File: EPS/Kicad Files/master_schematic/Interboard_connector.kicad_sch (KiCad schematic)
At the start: 1 part, among them J1 Conn_02x20_Odd_Even

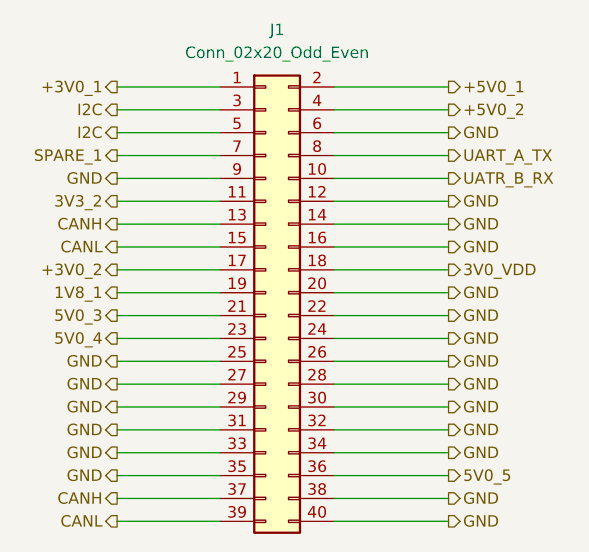
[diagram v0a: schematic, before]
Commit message: revised EPS schematics
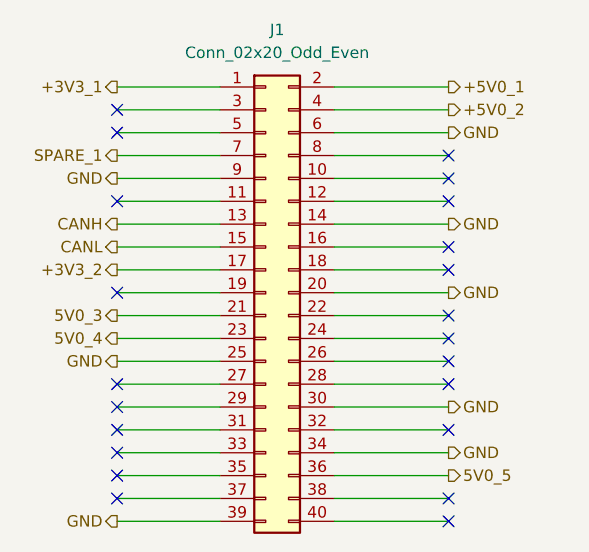
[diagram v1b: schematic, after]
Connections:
- net CANH: no longer J1.37 (Pin_37)
- net CANL: no longer J1.39 (Pin_39)
- net GND: now also J1.39 (Pin_39); no longer J1.12 (Pin_12), J1.16 (Pin_16), J1.22 (Pin_22), J1.24 (Pin_24), J1.26 (Pin_26), J1.27 (Pin_27), J1.28 (Pin_28), J1.29 (Pin_29), J1.31 (Pin_31), J1.32 (Pin_32), J1.33 (Pin_33), J1.35 (Pin_35), J1.38 (Pin_38), J1.40 (Pin_40)
- net +3V0_1 renamed +3V3_1
- net +3V0_2 renamed +3V3_2
- net 1V8_1: no longer names the net of J1.19 (Pin_19)
- net 3V0_VDD: no longer names the net of J1.18 (Pin_18)
- net 3V3_2: no longer names the net of J1.11 (Pin_11)
- net I2C: no longer names the net of J1.3 (Pin_3)
- net I2C: no longer J1.5 (Pin_5)
- net UART_A_TX: no longer names the net of J1.8 (Pin_8)
- net UATR_B_RX: no longer names the net of J1.10 (Pin_10)
- no-connect marks 0 -> 22
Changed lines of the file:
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@@
     (date "2022-01-27")
   )
+  (no_connect (at 106.68 76.2))
+  (no_connect (at 143.51 101.6))
+  (no_connect (at 143.51 73.66))
+  (no_connect (at 143.51 111.76))
+  (no_connect (at 143.51 109.22))
+  (no_connect (at 143.51 96.52))
+  (no_connect (at 143.51 93.98))
+  (no_connect (at 143.51 91.44))
+  (no_connect (at 143.51 88.9))
+  (no_connect (at 143.51 71.12))
+  (no_connect (at 143.51 81.28))
+  (no_connect (at 143.51 76.2))
+  (no_connect (at 106.68 68.58))
+  (no_connect (at 106.68 66.04))
+  (no_connect (at 106.68 96.52))
+  (no_connect (at 106.68 99.06))
+  (no_connect (at 106.68 101.6))
+  (no_connect (at 106.68 104.14))
+  (no_connect (at 106.68 106.68))
+  (no_connect (at 106.68 109.22))
+  (no_connect (at 106.68 86.36))
+  (no_connect (at 143.51 83.82))
   (wire (pts (xy 130.81 93.98) (xy 143.51 93.98))
     (stroke (width 0) (type default) (color 0 0 0 0))
@@
   )
   (wire (pts (xy 106.68 68.58) (xy 118.11 68.58))
-    (stroke (width 0) (type default) (color 0 0 0 0))
-  )
-  (wire (pts (xy 106.68 106.68) (xy 118.11 106.68))
     (stroke (width 0) (type default) (color 0 0 0 0))
   )
@@
   )
   (wire (pts (xy 130.81 73.66) (xy 143.51 73.66))
+    (stroke (width 0) (type default) (color 0 0 0 0))
+  )
+  (wire (pts (xy 118.11 106.68) (xy 106.68 106.68))
     (stroke (width 0) (type default) (color 0 0 0 0))
   )
@@
     (effects (font (size 1.27 1.27)) (justify right))
   )
-  (hierarchical_label "UATR_B_RX" (shape output) (at 143.51 73.66 0)
-    (effects (font (size 1.27 1.27)) (justify left))
-  )
-  (hierarchical_label "GND" (shape output) (at 106.68 104.14 180)
-    (effects (font (size 1.27 1.27)) (justify right))
-  )
-  (hierarchical_label "GND" (shape output) (at 143.51 101.6 0)
-    (effects (font (size 1.27 1.27)) (justify left))
-  )
   (hierarchical_label "GND" (shape output) (at 106.68 73.66 180)
     (effects (font (size 1.27 1.27)) (justify right))
@@
     (effects (font (size 1.27 1.27)) (justify right))
   )
-  (hierarchical_label "+3V0_2" (shape output) (at 106.68 83.82 180)
+  (hierarchical_label "+3V3_2" (shape output) (at 106.68 83.82 180)
     (effects (font (size 1.27 1.27)) (justify right))
-  )
-  (hierarchical_label "CANL" (shape output) (at 106.68 111.76 180)
-    (effects (font (size 1.27 1.27)) (justify right))
-  )
-  (hierarchical_label "GND" (shape output) (at 143.51 111.76 0)
-    (effects (font (size 1.27 1.27)) (justify left))
-  )
-  (hierarchical_label "GND" (shape output) (at 143.51 76.2 0)
-    (effects (font (size 1.27 1.27)) (justify left))
   )
   (hierarchical_label "GND" (shape output) (at 143.51 68.58 0)
@@
     (effects (font (size 1.27 1.27)) (justify right))
   )
-  (hierarchical_label "GND" (shape output) (at 143.51 91.44 0)
-    (effects (font (size 1.27 1.27)) (justify left))
-  )
   (hierarchical_label "5V0_4" (shape output) (at 106.68 91.44 180)
     (effects (font (size 1.27 1.27)) (justify right))
   )
-  (hierarchical_label "GND" (shape output) (at 143.51 88.9 0)
-    (effects (font (size 1.27 1.27)) (justify left))
-  )
   (hierarchical_label "+5V0_1" (shape output) (at 143.51 63.5 0)
-    (effects (font (size 1.27 1.27)) (justify left))
-  )
-  (hierarchical_label "GND" (shape output) (at 106.68 99.06 180)
-    (effects (font (size 1.27 1.27)) (justify right))
-  )
-  (hierarchical_label "GND" (shape output) (at 143.51 109.22 0)
     (effects (font (size 1.27 1.27)) (justify left))
   )
@@
     (effects (font (size 1.27 1.27)) (justify left))
   )
-  (hierarchical_label "1V8_1" (shape output) (at 106.68 86.36 180)
-    (effects (font (size 1.27 1.27)) (justify right))
-  )
   (hierarchical_label "+5V0_2" (shape output) (at 143.51 66.04 0)
     (effects (font (size 1.27 1.27)) (justify left))
   )
-  (hierarchical_label "GND" (shape output) (at 106.68 106.68 180)
+  (hierarchical_label "GND" (shape output) (at 106.68 111.76 180)
     (effects (font (size 1.27 1.27)) (justify right))
   )
@@
     (effects (font (size 1.27 1.27)) (justify left))
   )
-  (hierarchical_label "+3V0_1" (shape output) (at 106.68 63.5 180)
-    (effects (font (size 1.27 1.27)) (justify right))
-  )
-  (hierarchical_label "CANH" (shape output) (at 106.68 109.22 180)
+  (hierarchical_label "+3V3_1" (shape output) (at 106.68 63.5 180)
     (effects (font (size 1.27 1.27)) (justify right))
   )
@@
     (effects (font (size 1.27 1.27)) (justify right))
   )
-  (hierarchical_label "3V0_VDD" (shape output) (at 143.51 83.82 0)
-    (effects (font (size 1.27 1.27)) (justify left))
-  )
-  (hierarchical_label "GND" (shape output) (at 106.68 101.6 180)
-    (effects (font (size 1.27 1.27)) (justify right))
-  )
-  (hierarchical_label "GND" (shape output) (at 143.51 81.28 0)
+  (hierarchical_label "GND" (shape output) (at 143.51 99.06 0)
     (effects (font (size 1.27 1.27)) (justify left))
   )
@@
     (effects (font (size 1.27 1.27)) (justify right))
   )
-  (hierarchical_label "GND" (shape output) (at 143.51 93.98 0)
-    (effects (font (size 1.27 1.27)) (justify left))
-  )
-  (hierarchical_label "3V3_2" (shape output) (at 106.68 76.2 180)
-    (effects (font (size 1.27 1.27)) (justify right))
-  )
-  (hierarchical_label "GND" (shape output) (at 143.51 96.52 0)
-    (effects (font (size 1.27 1.27)) (justify left))
-  )
-  (hierarchical_label "I2C" (shape output) (at 106.68 66.04 180)
-    (effects (font (size 1.27 1.27)) (justify right))
-  )
-  (hierarchical_label "GND" (shape output) (at 143.51 99.06 0)
-    (effects (font (size 1.27 1.27)) (justify left))
-  )
-  (hierarchical_label "I2C" (shape output) (at 106.68 68.58 180)
-    (effects (font (size 1.27 1.27)) (justify right))
-  )
-  (hierarchical_label "GND" (shape output) (at 106.68 96.52 180)
-    (effects (font (size 1.27 1.27)) (justify right))
-  )
-  (hierarchical_label "UART_A_TX" (shape output) (at 143.51 71.12 0)
-    (effects (font (size 1.27 1.27)) (justify left))
-  )
   (symbol (lib_id "Connector_Generic:Conn_02x20_Odd_Even") (at 123.19 86.36 0) (unit 1)

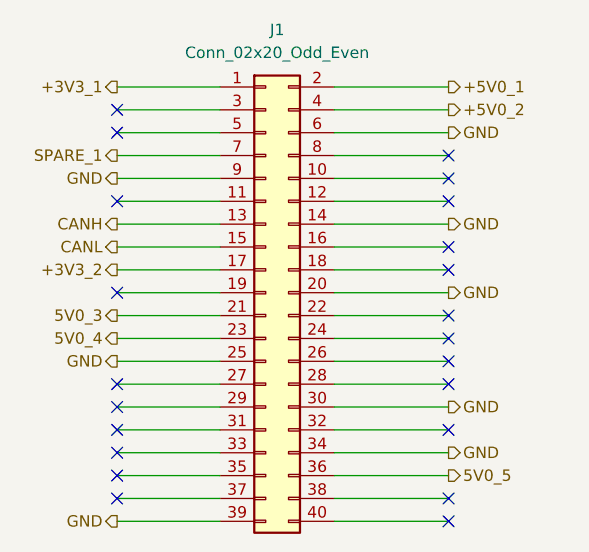
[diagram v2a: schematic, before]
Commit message: updated master schematic
should be nearing final schematic revision. run electrical rules check next
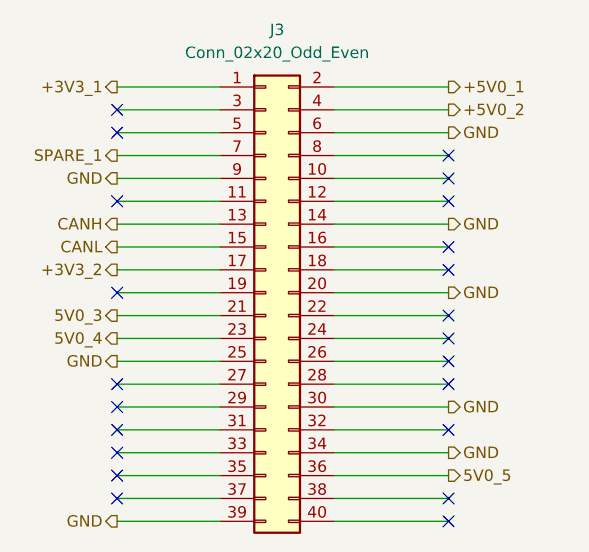
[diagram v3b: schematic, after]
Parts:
- renumbered J1 to J3
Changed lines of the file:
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@@
   (symbol (lib_id "Connector_Generic:Conn_02x20_Odd_Even") (at 123.19 86.36 0) (unit 1)
     (in_bom yes) (on_board yes) (fields_autoplaced)
-    (property "Reference" "J1" (id 0) (at 124.46 57.15 0))
+    (property "Reference" "J3" (id 0) (at 124.46 57.15 0))
     (property "Value" "Conn_02x20_Odd_Even" (id 1) (at 124.46 59.69 0))
     (property "Footprint" "Connector_PinHeader_2.54mm:PinHeader_2x20_P2.54mm_Vertical" (id 2) (at 123.19 86.36 0)
